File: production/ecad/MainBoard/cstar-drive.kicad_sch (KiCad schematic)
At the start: 58 parts, among them J1 B4B-PH-K-S, J10 Conn_01x03_Pin, J2 B4B-PH-K-S, J3 Conn_01x03_Pin, J4 Conn_01x03_Pin, J5 Conn_01x03_Pin, J6 Conn_01x03_Pin, J7 Conn_01x03_Pin, J8 Conn_01x03_Pin, J9 Conn_01x03_Pin, U1 DRV8842PWPR, U2 DRV8842PWPR, U3 STPS10L25G-TR, U4 STPS10L25G-TR, U5 STPS10L25G-TR, U6 STPS10L25G-TR, X1 B2P-VH, X2 B2P-VH

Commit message: "Aesthetics"
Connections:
- net OUT1 MOTOR 2 is gone; now on net GND: TP9.1, U2.10 (OUT1), U2.5 (OUT1)
- net OUT2 MOTOR 2 is gone; now on net GND: TP10.1, U2.7 (OUT2), U2.8 (OUT2)
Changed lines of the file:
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@@
-    (stroke (width 0) (type default))
-  )
-  (polyline (pts (xy 405.13 40.64) (xy 405.13 76.2))
     (stroke (width 0) (type default))
   )
@@
     (stroke (width 0) (type default))
   )
-  (polyline (pts (xy 405.13 76.2) (xy 405.13 250.19))
-    (stroke (width 0) (type default))
-  )
   (wire (pts (xy 189.23 151.13) (xy 194.31 151.13))
     (stroke (width 0) (type default))
@@
     (stroke (width 0) (type default))
   )
-  (polyline (pts (xy 403.86 250.19) (xy 405.13 250.19))
-    (stroke (width 0) (type default))
-  )
   (wire (pts (xy 44.45 146.05) (xy 71.12 146.05))
     (stroke (width 0) (type default))
@@
     (stroke (width 0) (type default))
   )
-  (polyline (pts (xy 259.08 40.64) (xy 405.13 40.64))
+  (polyline (pts (xy 259.08 40.64) (xy 328.93 40.64))
     (stroke (width 0) (type default))
   )
@@
     (effects (font (size 1.27 1.27)) (justify left bottom))
   )
-  (label "OUT1 MOTOR 1" (at 237.49 274.32 0) (fields_autoplaced)
+  (label "OUT1 MOTOR 2" (at 237.49 274.32 0) (fields_autoplaced)
     (effects (font (size 1.27 1.27)) (justify left bottom))
   )
@@
     (effects (font (size 1.27 1.27)) (justify left bottom))
   )
-  (label "OUT2 MOTOR 1" (at 210.82 241.3 0) (fields_autoplaced)
-    (effects (font (size 1.27 1.27)) (justify left bottom))
-  )
+  (label "OUT2 MOTOR 2" (at 210.82 241.3 0) (fields_autoplaced)
+    (effects (font (size 1.27 1.27)) (justify left bottom))
+  )

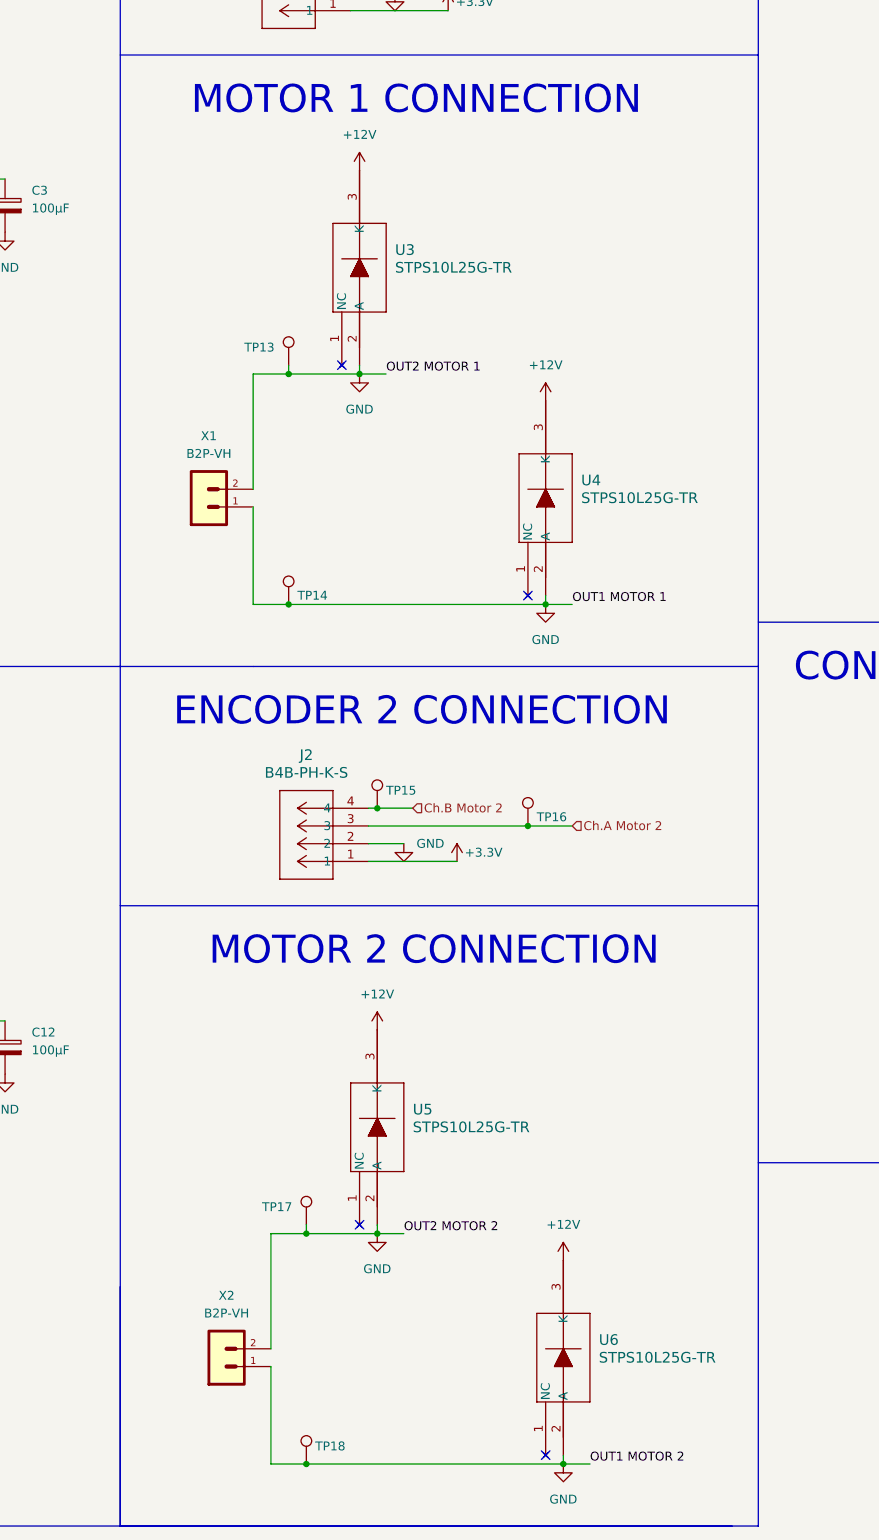
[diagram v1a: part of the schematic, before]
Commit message: "Fixed Motor Connectors"
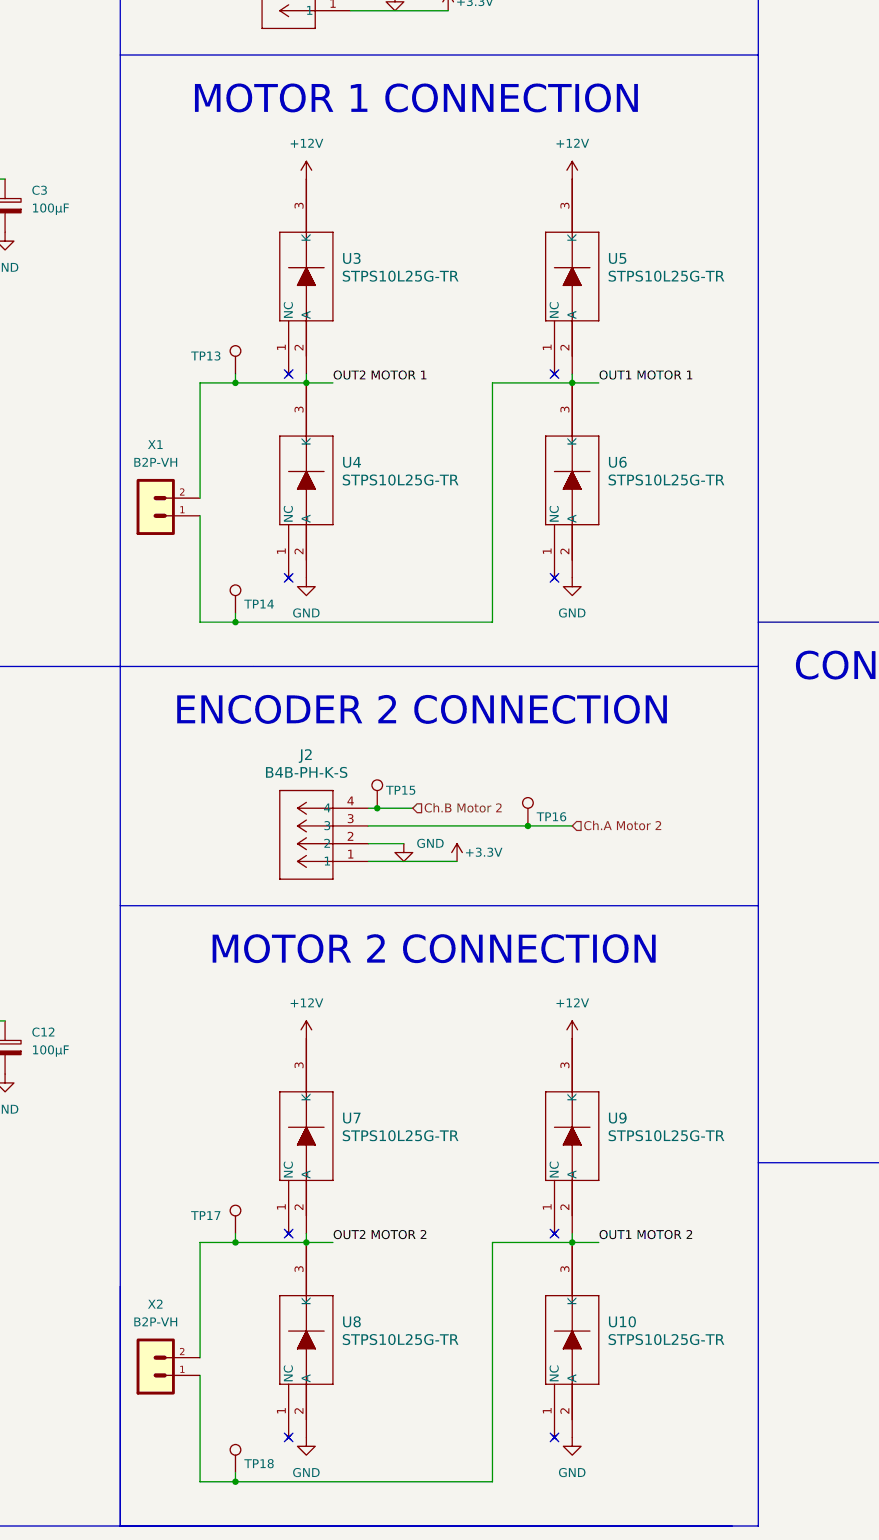
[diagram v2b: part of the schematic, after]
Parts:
- added U10, U7, U8, U9: STPS10L25G-TR, D2PAK_STM, symbol STPS10L25G-TR:STPS10L25G-TR
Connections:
- net +12V: now also U7.3 (K), U9.3 (K); no longer U4.3 (K), U6.3 (K)
- net GND: now also U10.2 (A), U8.2 (A); no longer TP10.1, TP13.1, TP14.1, TP17.1, TP18.1, TP4.1, TP5.1, TP9.1, U1.10 (OUT1), U1.5 (OUT1), U1.7 (OUT2), U1.8 (OUT2), U2.10 (OUT1), U2.5 (OUT1), U2.7 (OUT2), U2.8 (OUT2), U3.2 (A), U5.2 (A), X1.1, X1.2, X2.1, X2.2
- new net OUT1 MOTOR 1: TP14.1, TP4.1, U1.10 (OUT1), U1.5 (OUT1), U5.2 (A), U6.3 (K), X1.1
- new net OUT1 MOTOR 2: TP18.1, TP9.1, U10.3 (K), U2.10 (OUT1), U2.5 (OUT1), U9.2 (A), X2.1
- new net OUT2 MOTOR 1: TP13.1, TP5.1, U1.7 (OUT2), U1.8 (OUT2), U3.2 (A), U4.3 (K), X1.2
- new net OUT2 MOTOR 2: TP10.1, TP17.1, U2.7 (OUT2), U2.8 (OUT2), U7.2 (A), U8.3 (K), X2.2
- no-connect marks 6 -> 10
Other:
- moved on the sheet: TP13, TP14, U3, U4, X1

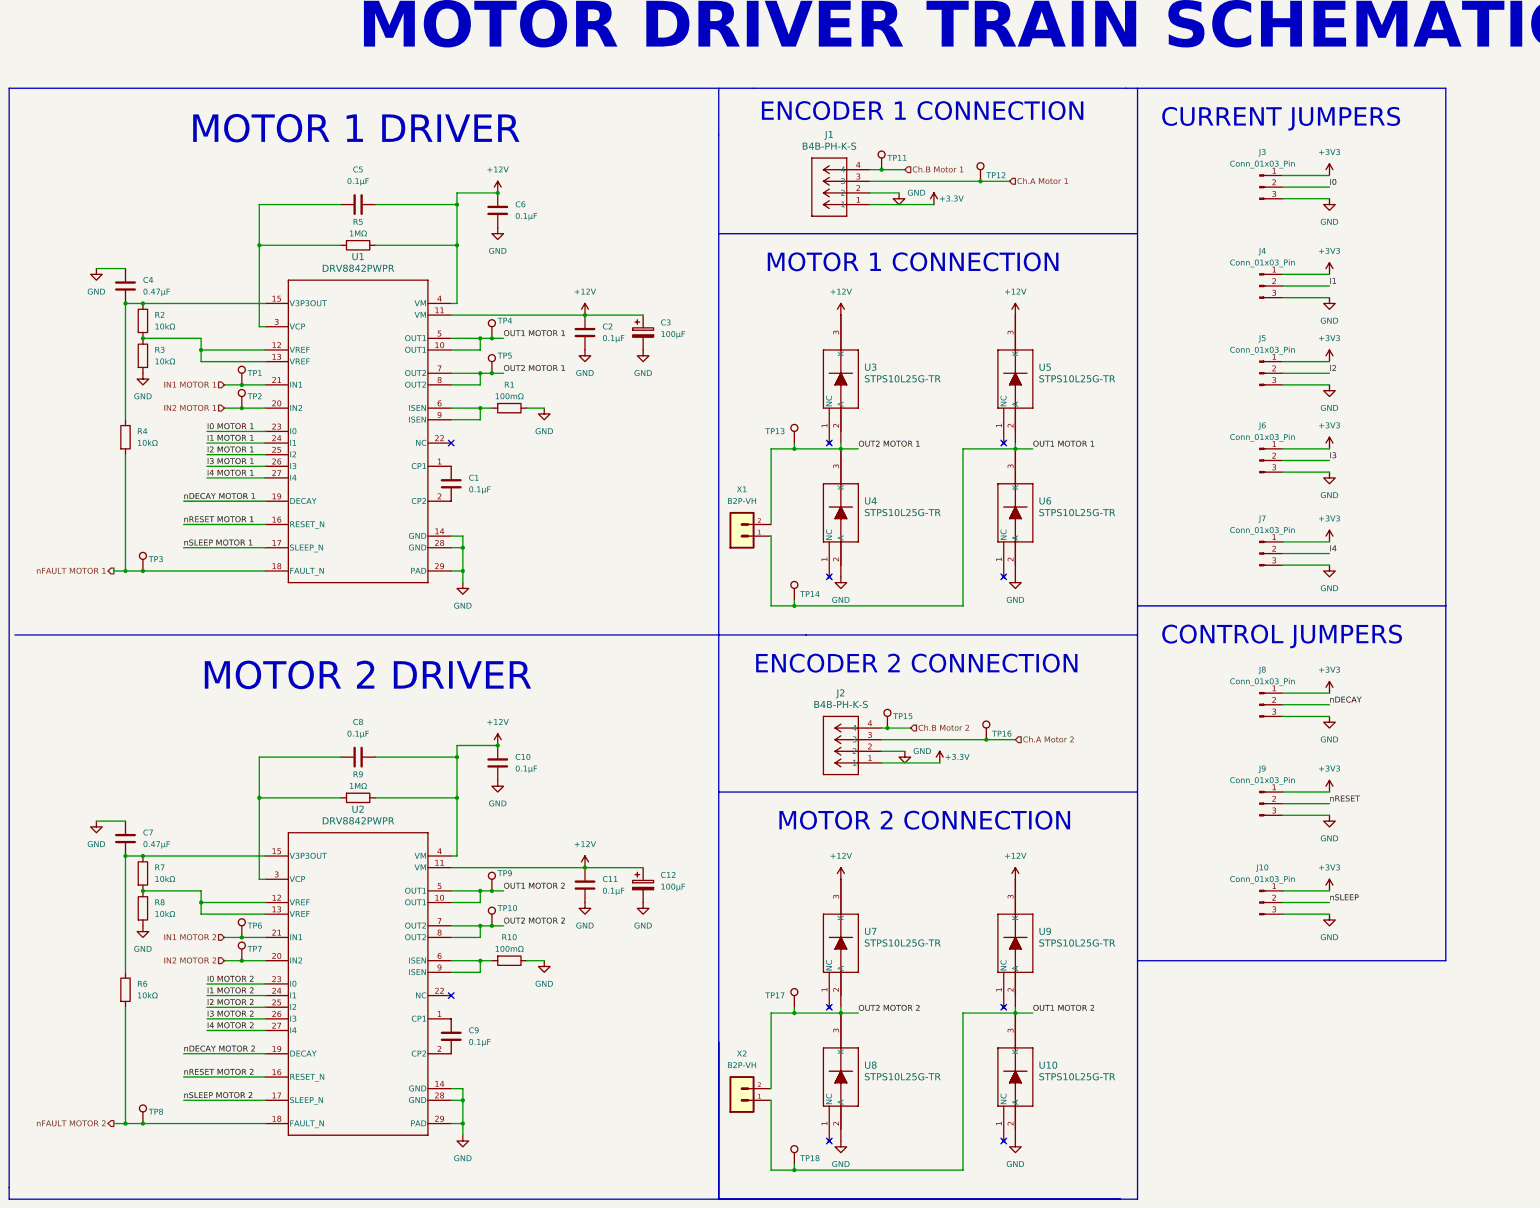
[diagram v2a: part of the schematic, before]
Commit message: "Removed Flyback Diodes"
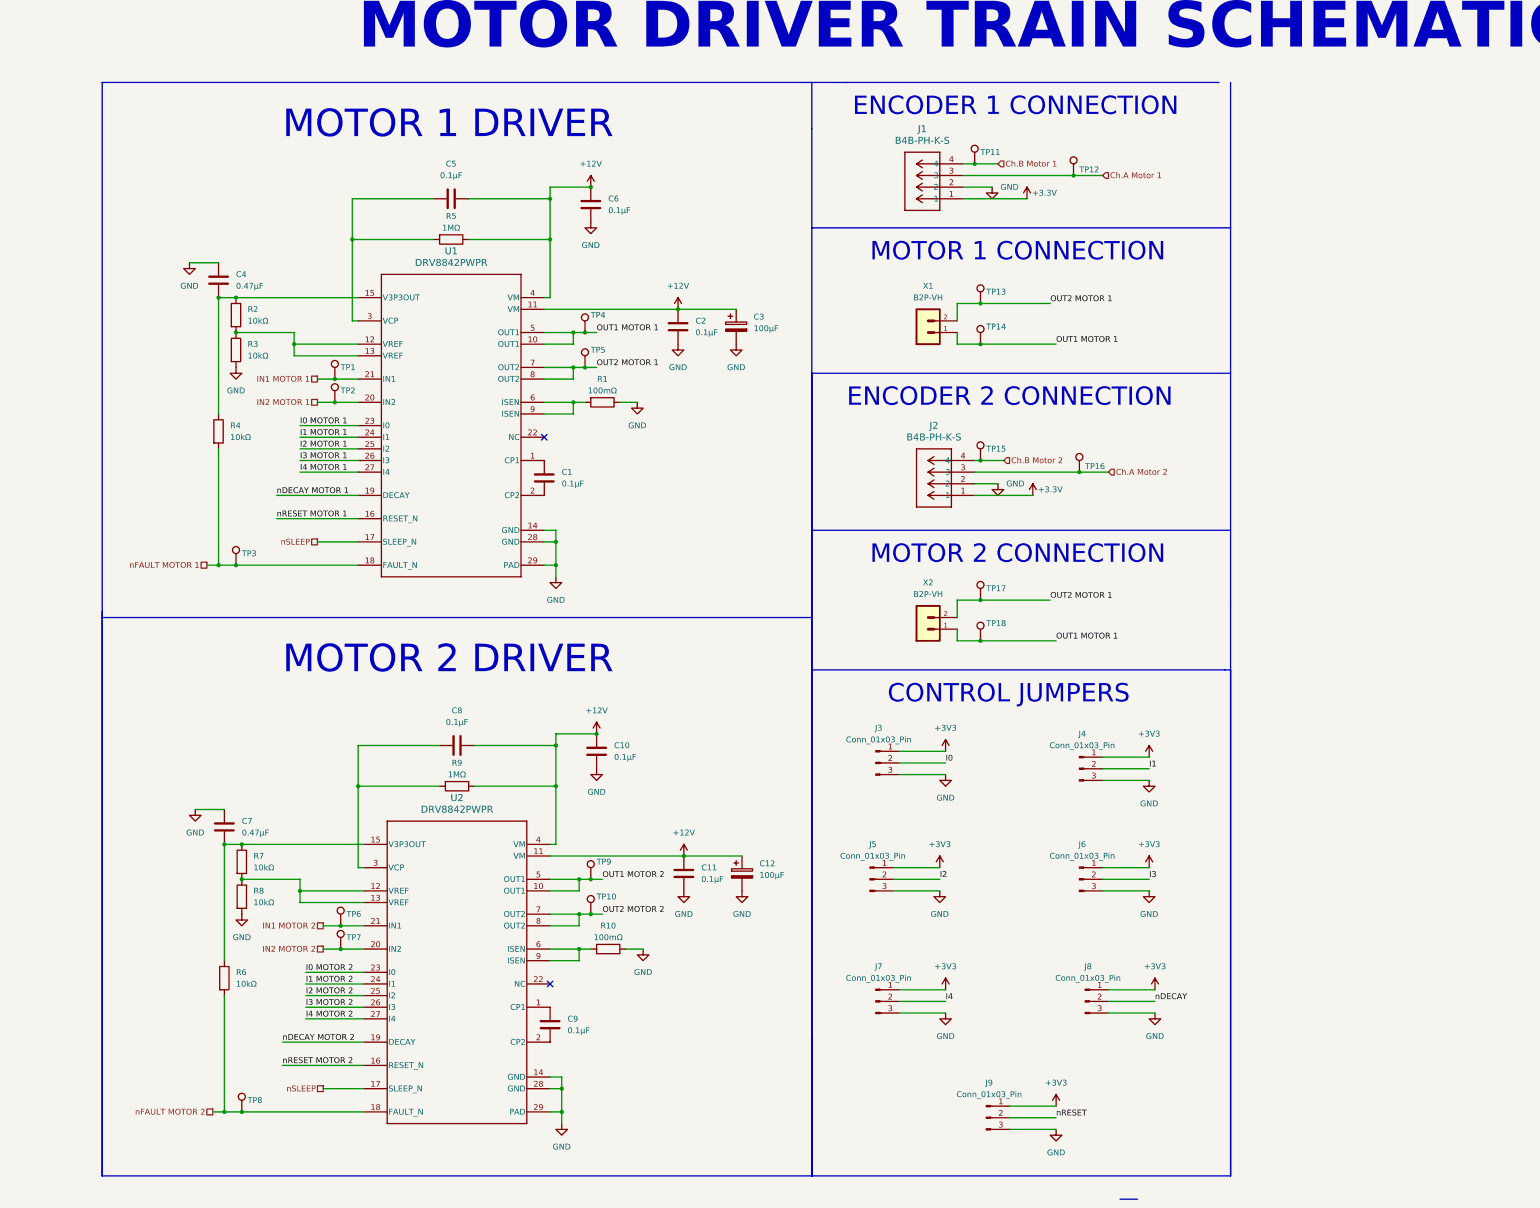
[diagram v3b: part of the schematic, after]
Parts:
- removed J10: Conn_01x03_Pin, symbol Connector:Conn_01x03_Pin
- removed U10, U3, U4, U5, U6, U7, U8, U9: STPS10L25G-TR, D2PAK_STM, symbol STPS10L25G-TR:STPS10L25G-TR
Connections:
- net nSLEEP MOTOR 1 is gone; now on net nSLEEP: U1.17 (SLEEP_N)
- net nSLEEP MOTOR 2 is gone; now on net nSLEEP: U2.17 (SLEEP_N)
- net OUT1 MOTOR 1: now also TP18.1, X2.1
- net OUT1 MOTOR 2: no longer TP18.1, X2.1
- net OUT2 MOTOR 1: now also TP17.1, X2.2
- net OUT2 MOTOR 2: no longer TP17.1, X2.2
- no-connect marks 10 -> 2
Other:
- note removed: "CURRENT JUMPERS"
- moved on the sheet: C1, C10, C11, C12, C2, C3, C4, C5, C6, C7, C8, C9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

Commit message: "Fixed Net Names"
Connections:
- net I0 MOTOR 1 is gone; now on net I0: U1.23 (I0)
- net I0 MOTOR 2 is gone; now on net I0: U2.23 (I0)
- net I1 MOTOR 1 is gone; now on net I1: U1.24 (I1)
- net I1 MOTOR 2 is gone; now on net I1: U2.24 (I1)
- net I2 MOTOR 1 is gone; now on net I2: U1.25 (I2)
- net I2 MOTOR 2 is gone; now on net I2: U2.25 (I2)
- net I3 MOTOR 1 is gone; now on net I3: U1.26 (I3)
- net I3 MOTOR 2 is gone; now on net I3: U2.26 (I3)
- net I4 MOTOR 1 is gone; now on net I4: U1.27 (I4)
- net I4 MOTOR 2 is gone; now on net I4: U2.27 (I4)
- net nDECAY MOTOR 1 is gone; now on net nDECAY: U1.19 (DECAY)
- net nDECAY MOTOR 2 is gone; now on net nDECAY: U2.19 (DECAY)
- net nRESET MOTOR 1 is gone; now on net nRESET: U1.16 (RESET_N)
- net nRESET MOTOR 2 is gone; now on net nRESET: U2.16 (RESET_N)
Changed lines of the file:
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@@
     (stroke (width 0) (type default))
   )
-  (wire (pts (xy 82.55 139.7) (xy 91.44 139.7))
+  (wire (pts (xy 87.63 139.7) (xy 91.44 139.7))
     (stroke (width 0) (type default))
   )
@@
     (stroke (width 0) (type default))
   )
-  (wire (pts (xy 83.82 259.08) (xy 92.71 259.08))
+  (wire (pts (xy 88.9 259.08) (xy 92.71 259.08))
     (stroke (width 0) (type default))
   )
@@
     (stroke (width 0) (type default))
   )
-  (wire (pts (xy 74.93 248.92) (xy 92.71 248.92))
+  (wire (pts (xy 80.01 248.92) (xy 92.71 248.92))
     (stroke (width 0) (type default))
   )
@@
     (stroke (width 0) (type default))
   )
-  (wire (pts (xy 73.66 134.62) (xy 91.44 134.62))
+  (wire (pts (xy 78.74 134.62) (xy 91.44 134.62))
     (stroke (width 0) (type default))
   )
@@
     (stroke (width 0) (type default))
   )
+  (polyline (pts (xy 279.4 39.37) (xy 281.94 39.37))
+    (stroke (width 0) (type default))
+  )
   (wire (pts (xy 226.06 127) (xy 231.14 127))
     (stroke (width 0) (type default))
@@
     (stroke (width 0) (type default))
   )
-  (wire (pts (xy 73.66 129.54) (xy 91.44 129.54))
+  (wire (pts (xy 78.74 129.54) (xy 91.44 129.54))
     (stroke (width 0) (type default))
   )
@@
     (stroke (width 0) (type default))
   )
-  (wire (pts (xy 74.93 254) (xy 92.71 254))
+  (wire (pts (xy 80.01 254) (xy 92.71 254))
     (stroke (width 0) (type default))
   )
@@
     (effects (font (size 1.27 1.27)) (justify left bottom))
   )
-  (label "nRESET MOTOR 1" (at 73.66 134.62 0) (fields_autoplaced)
-    (effects (font (size 1.27 1.27)) (justify left bottom))
-  )
-  (label "nDECAY MOTOR 2" (at 74.93 248.92 0) (fields_autoplaced)
-    (effects (font (size 1.27 1.27)) (justify left bottom))
-  )
-  (label "I4 MOTOR 1" (at 78.74 124.46 0) (fields_autoplaced)
-    (effects (font (size 1.27 1.27)) (justify left bottom))
-  )
-  (label "I1 MOTOR 2" (at 80.01 236.22 0) (fields_autoplaced)
-    (effects (font (size 1.27 1.27)) (justify left bottom))
-  )
-  (label "I3 MOTOR 1" (at 78.74 121.92 0) (fields_autoplaced)
-    (effects (font (size 1.27 1.27)) (justify left bottom))
-  )
-  (label "I2 MOTOR 2" (at 80.01 238.76 0) (fields_autoplaced)
+  (label "nRESET" (at 78.74 134.62 0) (fields_autoplaced)
+    (effects (font (size 1.27 1.27)) (justify left bottom))
+  )
+  (label "nDECAY" (at 80.01 248.92 0) (fields_autoplaced)
+    (effects (font (size 1.27 1.27)) (justify left bottom))
+  )
+  (label "I4" (at 78.74 124.46 0) (fields_autoplaced)
+    (effects (font (size 1.27 1.27)) (justify left bottom))
+  )
+  (label "I1" (at 80.01 236.22 0) (fields_autoplaced)
+    (effects (font (size 1.27 1.27)) (justify left bottom))
+  )
+  (label "I3" (at 78.74 121.92 0) (fields_autoplaced)
+    (effects (font (size 1.27 1.27)) (justify left bottom))
+  )
+  (label "I2" (at 80.01 238.76 0) (fields_autoplaced)
     (effects (font (size 1.27 1.27)) (justify left bottom))
   )
@@
     (effects (font (size 1.27 1.27)) (justify left bottom))
   )
-  (label "I2 MOTOR 1" (at 78.74 119.38 0) (fields_autoplaced)
-    (effects (font (size 1.27 1.27)) (justify left bottom))
-  )
-  (label "I3 MOTOR 2" (at 80.01 241.3 0) (fields_autoplaced)
+  (label "I2" (at 78.74 119.38 0) (fields_autoplaced)
+    (effects (font (size 1.27 1.27)) (justify left bottom))
+  )
+  (label "I3" (at 80.01 241.3 0) (fields_autoplaced)
     (effects (font (size 1.27 1.27)) (justify left bottom))
   )
@@
     (effects (font (size 1.27 1.27)) (justify left bottom))
   )
-  (label "I0 MOTOR 1" (at 78.74 114.3 0) (fields_autoplaced)
+  (label "I0" (at 78.74 114.3 0) (fields_autoplaced)
     (effects (font (size 1.27 1.27)) (justify left bottom))
   )
@@
     (effects (font (size 1.27 1.27)) (justify left bottom))
   )
-  (label "nDECAY MOTOR 1" (at 73.66 129.54 0) (fields_autoplaced)
-    (effects (font (size 1.27 1.27)) (justify left bottom))
-  )
-  (label "nRESET MOTOR 2" (at 74.93 254 0) (fields_autoplaced)
+  (label "nDECAY" (at 78.74 129.54 0) (fields_autoplaced)
+    (effects (font (size 1.27 1.27)) (justify left bottom))
+  )
+  (label "nRESET" (at 80.01 254 0) (fields_autoplaced)
     (effects (font (size 1.27 1.27)) (justify left bottom))
   )
@@
     (effects (font (size 1.27 1.27)) (justify left bottom))
   )
-  (label "I0 MOTOR 2" (at 80.01 233.68 0) (fields_autoplaced)
-    (effects (font (size 1.27 1.27)) (justify left bottom))
-  )
-  (label "I1 MOTOR 1" (at 78.74 116.84 0) (fields_autoplaced)
+  (label "I0" (at 80.01 233.68 0) (fields_autoplaced)
+    (effects (font (size 1.27 1.27)) (justify left bottom))
+  )
+  (label "I1" (at 78.74 116.84 0) (fields_autoplaced)
     (effects (font (size 1.27 1.27)) (justify left bottom))
   )
@@
     (effects (font (size 1.27 1.27)) (justify left bottom))
   )
-  (label "I4 MOTOR 2" (at 80.01 243.84 0) (fields_autoplaced)
+  (label "I4" (at 80.01 243.84 0) (fields_autoplaced)
     (effects (font (size 1.27 1.27)) (justify left bottom))
   )
@@
     (effects (font (size 1.27 1.27)) (justify right))
   )
-  (hierarchical_label "nSLEEP" (shape passive) (at 82.55 139.7 180) (fields_autoplaced)
+  (hierarchical_label "nSLEEP" (shape passive) (at 87.63 139.7 180) (fields_autoplaced)
     (effects (font (size 1.27 1.27)) (justify right))
   )
@@
     (effects (font (size 1.27 1.27)) (justify right))
   )
-  (hierarchical_label "nSLEEP" (shape passive) (at 83.82 259.08 180) (fields_autoplaced)
-    (effects (font (size 1.27 1.27)) (justify right))
-  )
+  (hierarchical_label "nSLEEP" (shape passive) (at 88.9 259.08 180) (fields_autoplaced)
+    (effects (font (size 1.27 1.27)) (justify right))
+  )
